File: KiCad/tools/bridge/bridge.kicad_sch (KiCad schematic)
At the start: 56 parts, among them J1 XF2J-1824-12A, J2 XF2J-1824-12A

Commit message: lot of modification, preparing a refactor + some rendering
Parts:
- J1, J2: LCSC (none) -> C397324
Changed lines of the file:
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@@
       (effects (font (size 1.524 1.524)))
+    )
+    (property "LCSC" "C397324" (id 4) (at 102.87 52.07 0)
+      (effects (font (size 1.27 1.27)) hide)
     )
     (pin "1")
@@
       (effects (font (size 1.524 1.524)))
     )
+    (property "LCSC" "C397324" (id 4) (at 62.23 52.07 0)
+      (effects (font (size 1.27 1.27)) hide)
+    )
     (pin "1")

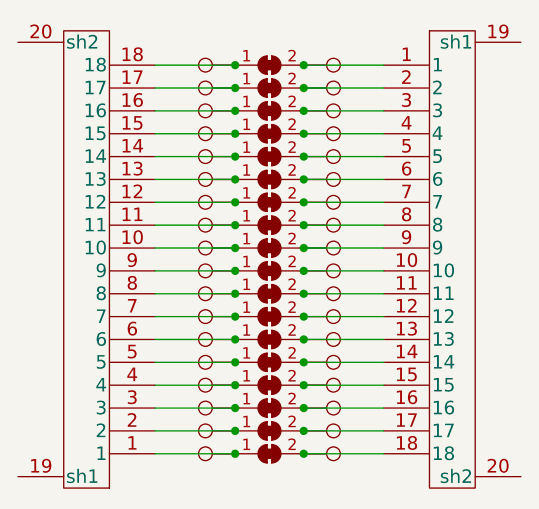
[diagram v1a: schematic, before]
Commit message: updated bridge
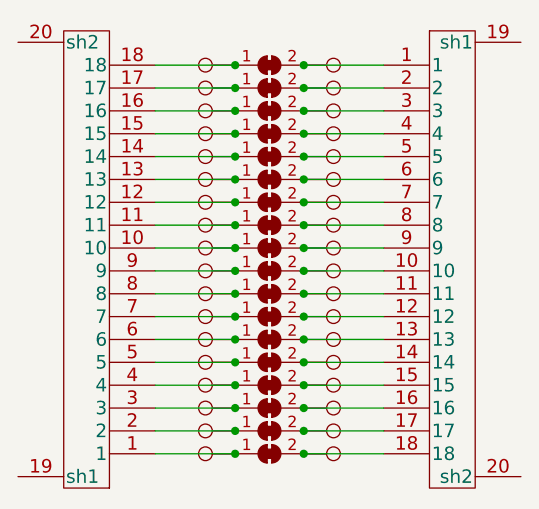
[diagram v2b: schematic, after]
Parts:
- JP1: footprint (none) -> Jumper:SolderJumper-2_P1.3mm_Bridged_RoundedPad1.0x1.5mm
- TP1: footprint (none) -> Connector_PinHeader_2.54mm:PinHeader_1x01_P2.54mm_Vertical
- TP10, TP11, TP12, TP13, TP14, TP15, TP16, TP17, TP18, TP19, TP2, TP20, TP21, TP22, TP23, TP24, TP25, TP26, TP27, TP28, TP29, TP3, TP30, TP31, TP32, TP33, TP34, TP35, TP36, TP4, TP5, TP6, TP7, TP8, TP9: footprint Connector_Pin:Pin_D0.7mm_L6.5mm_W1.8mm_FlatFork -> Connector_PinHeader_2.54mm:PinHeader_1x01_P2.54mm_Vertical
